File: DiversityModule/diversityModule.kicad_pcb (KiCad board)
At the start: 2 copper layers, 56.5 x 25 mm, 42 parts, among them IC1 LP38798, IC2 TDA1308A, P1 CONN_02X05, P2 CONN_01X03, Q1 BFP840, U1 sn74lvc1g3157, U2 RX5808

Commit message: BOM für beide platinen des kompletten moduls dazugefügt
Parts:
- SMA_E1: footprint PhilippsFootprints:SMA_EDGE_small -> PhilippsFootprints:SMA_EDGE_Johnson_142-0701-801
- moved SMA_E1 0.80 mm to (85.9, 86.7)
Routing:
- net Net-(C15-Pad1): track 5.55 -> 11.3 mm
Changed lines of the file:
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@@
     (links 104)
     (no_connects 0)
-    (area 91.924999 79.924999 148.575001 105.075001)
+    (area 79.159499 79.5 157.35 109.200001)
     (thickness 1.6)
     (drawings 9)
-    (tracks 414)
+    (tracks 418)
     (zones 0)
     (modules 42)
@@
     (34 B.Paste user)
     (35 F.Paste user)
-    (36 B.SilkS user hide)
+    (36 B.SilkS user)
     (37 F.SilkS user)
     (38 B.Mask user)
@@
     (visible_elements FFFEFF7F)
     (pcbplotparams
-      (layerselection 0x00030_ffffffff)
-      (usegerberextensions false)
+      (layerselection 0x014f0_ffffffff)
+      (usegerberextensions true)
       (excludeedgelayer true)
       (linewidth 0.100000)
@@
       (psa4output false)
       (plotreference true)
-      (plotvalue true)
+      (plotvalue false)
       (plotinvisibletext false)
       (padsonsilk false)
-      (subtractmaskfromsilk false)
+      (subtractmaskfromsilk true)
       (outputformat 1)
       (mirror false)
-      (drillshape 1)
+      (drillshape 0)
       (scaleselection 1)
-      (outputdirectory ""))
+      (outputdirectory gerber/))
   )
   (net 0 "")
@@
     )
   )
-  (module PhilippsFootprints:SMA_EDGE_small (layer B.Cu)
-    (at 85.9 85.9 180)
-    (fp_text reference SMA_E1 (at 0 0 180) (layer B.SilkS) hide
-      (effects (font (thickness 0.3048)) (justify mirror))
-    )
-    (fp_text value SMA_EDGE (at 0 -2.54 180) (layer B.SilkS) hide
-      (effects (font (thickness 0.3048)) (justify mirror))
-    )
-    (fp_line (start -6.35 2.5654) (end -6.35 -5.0546) (layer B.SilkS) (width 0.381))
-    (fp_line (start -6.35 -5.0546) (end 6.35 -5.0546) (layer B.SilkS) (width 0.381))
-    (fp_line (start 6.35 -5.0546) (end 6.35 2.5654) (layer B.SilkS) (width 0.381))
-    (fp_line (start 6.35 2.5654) (end -6.35 2.5654) (layer B.SilkS) (width 0.381))
-    (pad 0 connect rect (at -8.8773 1.89484 180) (size 4.572 1.524) (layers *.Cu B.Mask)
-      (net 2 GNDA))
-    (pad 1 connect trapezoid (at -6.858 -1.27 180) (size 0.50038 1.39954) (rect_delta 0.59944 0 ) (layers F.Cu F.Mask)
-      (net 17 "Net-(C15-Pad1)"))
-    (pad 2 connect rect (at -8.8773 -4.42976 180) (size 4.572 1.524) (layers *.Cu B.Mask)
-      (net 2 GNDA))
-    (pad 1 connect rect (at -9.144 -1.27 180) (size 4.07162 1.99898) (layers F.Cu F.Mask)
-      (net 17 "Net-(C15-Pad1)"))
-    (model SMA_EDGE.wrl
-      (at (xyz -0.205 -0.05 -0.12))
-      (scale (xyz 1.3 1.3 1.3))
-      (rotate (xyz 270 0 180))
-    )
-  )
   (module PhilippsFootprints:RX5808 (layer B.Cu)
     (at 124.5 92.7)
@@
     (pad 1 smd rect (at 1.15 2) (size 1.3 2) (layers F.Cu F.Paste F.Mask)
       (net 32 "Net-(RV1-Pad1)"))
+  )
+  (module PhilippsFootprints:SMA_EDGE_Johnson_142-0701-801 (layer B.Cu)
+    (at 85.9 86.7 180)
+    (fp_text reference SMA_E1 (at 0 1.3 180) (layer B.SilkS)
+      (effects (font (thickness 0.3048)) (justify mirror))
+    )
+    (fp_text value SMA_EDGE (at 0 -1.24 180) (layer B.SilkS) hide
+      (effects (font (thickness 0.3048)) (justify mirror))
+    )
+    (fp_line (start -6.2 5.6) (end -6.3 5.6) (layer B.SilkS) (width 0.15))
+    (fp_line (start -6.3 5.6) (end -11.2 5.6) (layer B.SilkS) (width 0.15))
+    (fp_line (start -11.2 5.6) (end -11.2 -5.6) (layer B.SilkS) (width 0.15))
+    (fp_line (start -11.2 -5.6) (end -6.2 -5.6) (layer B.SilkS) (width 0.15))
+    (fp_line (start -6.2 -5.6) (end -6.2 5.6) (layer B.SilkS) (width 0.15))
+    (fp_line (start -6.35 3.8654) (end -6.35 -3.7546) (layer B.SilkS) (width 0.381))
+    (fp_line (start -6.35 -3.7546) (end 6.35 -3.7546) (layer B.SilkS) (width 0.381))
+    (fp_line (start 6.35 -3.7546) (end 6.35 3.8654) (layer B.SilkS) (width 0.381))
+    (fp_line (start 6.35 3.8654) (end -6.35 3.8654) (layer B.SilkS) (width 0.381))
+    (pad 0 connect rect (at -8.9 4.4 180) (size 4.572 2.413) (layers *.Mask F.Cu)
+      (net 2 GNDA))
+    (pad 1 connect trapezoid (at -6.858 0.03 180) (size 0.50038 1.39954) (rect_delta 0.59944 0 ) (layers F.Cu F.Mask)
+      (net 17 "Net-(C15-Pad1)"))
+    (pad 2 connect rect (at -8.9 -4.4 180) (size 4.572 2.413) (layers *.Mask F.Cu)
+      (net 2 GNDA))
+    (pad 1 connect rect (at -9.144 0.03 180) (size 4.07162 2.2) (layers F.Cu F.Mask)
+      (net 17 "Net-(C15-Pad1)"))
+    (model SMA_EDGE.wrl
+      (at (xyz -0.205 -0.05 -0.12))
+      (scale (xyz 1.3 1.3 1.3))
+      (rotate (xyz 270 0 180))
+    )
   )
   (dimension 25 (width 0.3) (layer Cmts.User)
@@
   (segment (start 101.5 90.05) (end 101.5 91) (width 0.15) (layer F.Cu) (net 16))
   (segment (start 105.9 90.55) (end 105.9 90.6) (width 0.15) (layer F.Cu) (net 16))
+  (segment (start 95.044 86.67) (end 96.57 86.67) (width 0.25) (layer F.Cu) (net 17))
+  (segment (start 96.57 86.67) (end 97.1 87.2) (width 0.25) (layer F.Cu) (net 17))
+  (segment (start 97.1 87.2) (end 98.25 87.2) (width 0.25) (layer F.Cu) (net 17))
+  (segment (start 92.758 86.67) (end 95.044 86.67) (width 0.25) (layer F.Cu) (net 17))
   (segment (start 98.25 87.2) (end 95.074 87.2) (width 0.786937) (layer F.Cu) (net 17))
   (segment (start 95.074 87.2) (end 95.044 87.17) (width 0.786937) (layer F.Cu) (net 17))

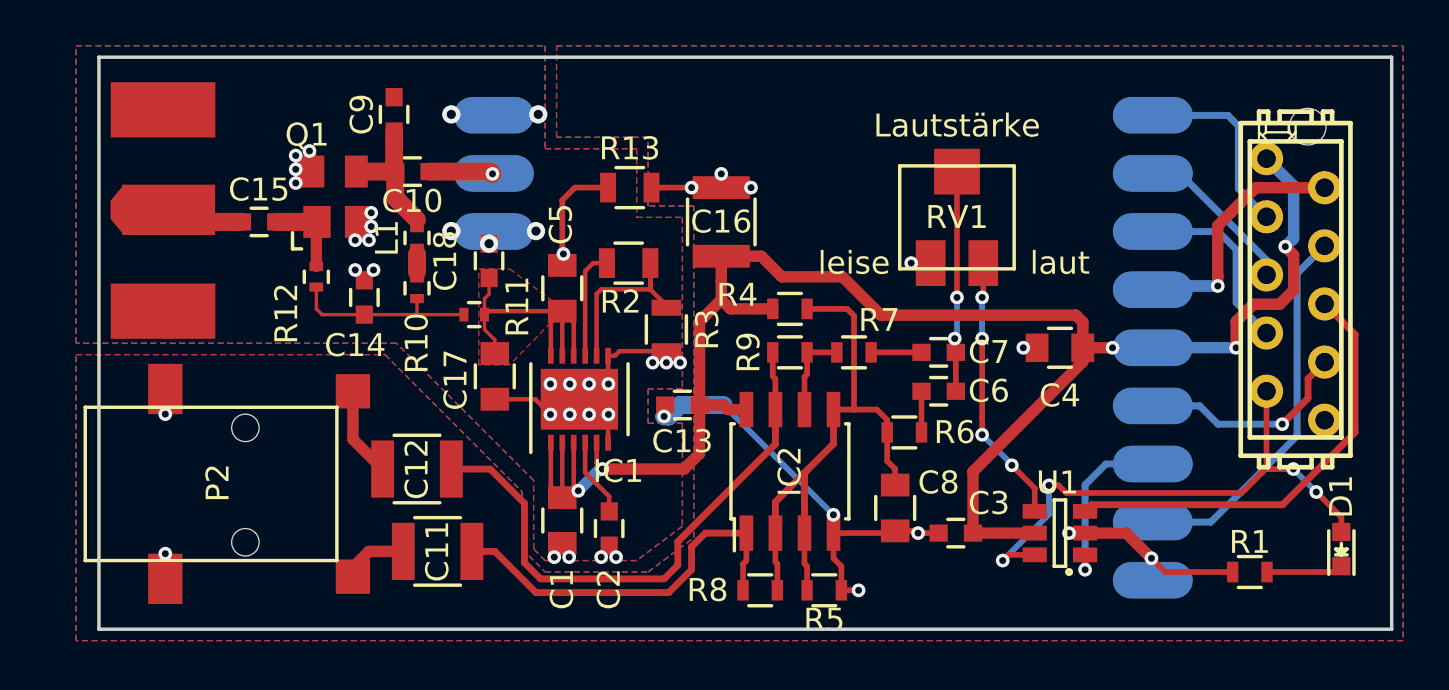
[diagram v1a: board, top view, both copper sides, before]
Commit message: Layoutänderungen für videoumschalter (anderes gehäuse)
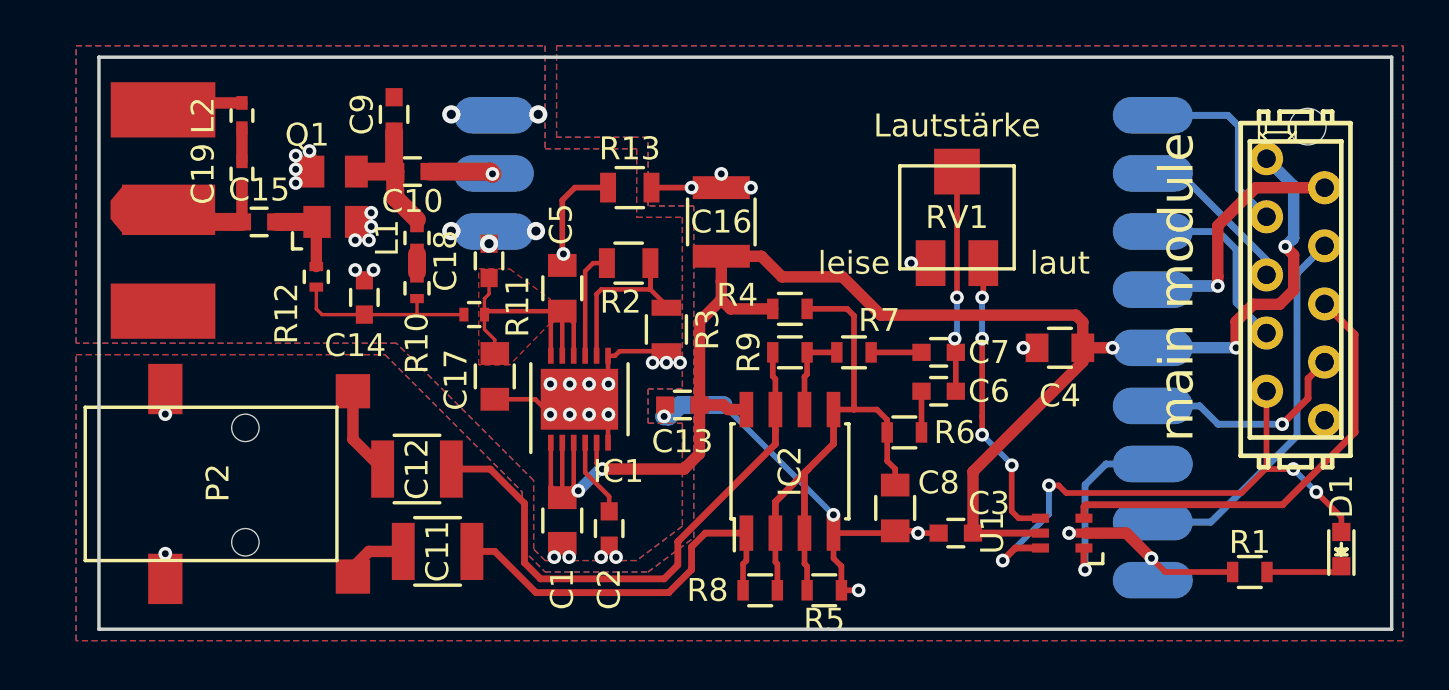
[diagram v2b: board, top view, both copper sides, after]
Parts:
- added C19: 2,2pF, Capacitors_SMD:C_0402, F.Cu at (98.2, 85.1)
- added L2: 1,8nH, Capacitors_SMD:C_0402, F.Cu at (98.2, 82.5)
- U1: footprint TO_SOT_Packages_SMD:SOT-23-6 -> TO_SOT_Packages_SMD:SC-70-6
- moved U1 0.10 mm to (134.1, 100.8), turned to 90 degrees
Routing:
- net GNDA: track 43.1 -> 46.7 mm
- net Net-(C15-Pad1): track 11.3 -> 12.8 mm
- net Net-(C19-Pad2): track 0.00 -> 1.45 mm
- net Net-(RV1-Pad1): track 11.8 -> 12.8 mm
- net /switch: track 23.9 -> 24.6 mm
- net GND: track 47.3 -> 48.0 mm
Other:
- board text added: "main module"

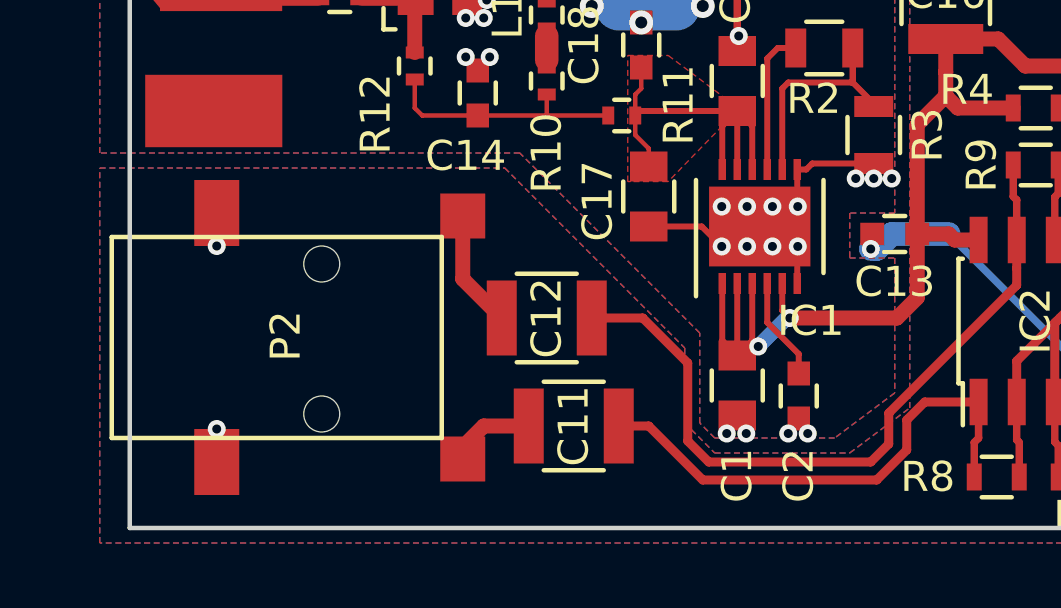
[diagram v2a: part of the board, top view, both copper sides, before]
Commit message: Klinkenbuchse ausgetauscht und zur Lib hinzugefügt.
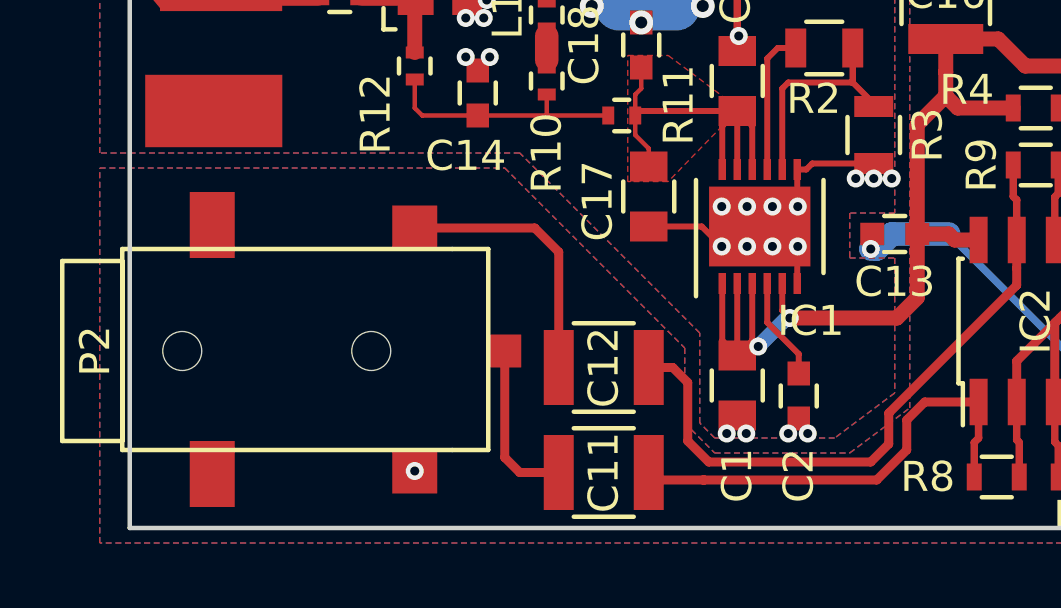
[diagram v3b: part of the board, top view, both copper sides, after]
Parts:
- P2: footprint PhilippsFootprints:LUM1503-SMD -> PhilippsFootprints:LUM1503-03
- moved C12 2.52 mm to (107.8, 99.7)
- moved C11 1.84 mm to (107.8, 103.2)
- moved P2 0.53 mm to (97.3, 99.1)
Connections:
- P2 pad 1: Net-(C12-Pad2) -> GND
- P2 pad 2: GND -> Net-(C11-Pad2)
- P2 pad 3: Net-(C11-Pad2) -> Net-(C12-Pad2)
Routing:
- net Net-(C12-Pad2): track 3.94 -> 8.98 mm
- net Net-(C12-Pad1): track 24.8 -> 21.8 mm
- net Net-(C11-Pad2): track 2.89 -> 5.56 mm
- net GND: track 48.0 -> 45.8 mm, vias 14 -> 13
- net Net-(C11-Pad1): track 17.0 -> 15.4 mm
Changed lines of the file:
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@@
 (kicad_pcb (version 4) (host pcbnew "(2016-06-07 BZR 6887)-product")
   (general
-    (links 107)
+    (links 106)
     (no_connects 0)
-    (area 91.924999 79.924999 148.575001 105.075001)
+    (area 79.159499 79.5 157.500001 109.245001)
     (thickness 1.6)
     (drawings 10)
-    (tracks 428)
+    (tracks 427)
     (zones 0)
     (modules 44)
@@
   )
   (setup
-    (last_trace_width 0.5)
+    (last_trace_width 0.3)
     (user_trace_width 0.15)
     (user_trace_width 0.2)
@@
   )
   (module Capacitors_SMD:C_1210 (layer F.Cu)
-    (at 106.8 101.6 180)
+    (at 107.8 103.15 180)
     (descr "Capacitor SMD 1210, reflow soldering, AVX (see smccp.pdf)")
     (tags "capacitor 1210")
@@
   )
   (module Capacitors_SMD:C_1210 (layer F.Cu)
-    (at 105.9 98 180)
+    (at 107.8 99.65 180)
     (descr "Capacitor SMD 1210, reflow soldering, AVX (see smccp.pdf)")
     (tags "capacitor 1210")
@@
       (net 4 GND))
   )
-  (module PhilippsFootprints:LUM1503-SMD (layer F.Cu)
-    (at 97 98.7)
-    (fp_text reference P2 (at 0.2 -0.1 90) (layer F.SilkS)
-      (effects (font (size 1 1) (thickness 0.15)))
-    )
-    (fp_text value CONN_01X03 (at -0.1 0.06) (layer F.Fab)
-      (effects (font (size 1 1) (thickness 0.15)))
-    )
-    (fp_line (start -5.6 -3.4) (end -5.6 3.3) (layer F.SilkS) (width 0.15))
-    (fp_line (start -5.6 3.3) (end 5.4 3.3) (layer F.SilkS) (width 0.15))
-    (fp_line (start 5.4 3.3) (end 5.4 -3.4) (layer F.SilkS) (width 0.15))
-    (fp_line (start 5.4 -3.4) (end -5.6 -3.4) (layer F.SilkS) (width 0.15))
-    (pad 3 smd rect (at 6.1 4) (size 1.5 1.5) (layers F.Cu F.Paste F.Mask)
-      (net 13 "Net-(C11-Pad2)"))
-    (pad 1 smd rect (at 6.1 -4.1) (size 1.5 1.5) (layers F.Cu F.Paste F.Mask)
-      (net 15 "Net-(C12-Pad2)"))
-    (pad 2 smd rect (at -2.1 4.1) (size 1.5 2.2) (layers F.Cu F.Paste F.Mask)
-      (net 4 GND))
-    (pad 2 smd rect (at -2.1 -4.2) (size 1.5 2.2) (layers F.Cu F.Paste F.Mask)
-      (net 4 GND))
-    (pad "" np_thru_hole circle (at 1.4 -2.5) (size 1.2 1.2) (drill 1.2) (layers *.Cu *.Mask F.SilkS))
-    (pad "" np_thru_hole circle (at 1.4 2.5) (size 1.2 1.2) (drill 1.2) (layers *.Cu *.Mask F.SilkS))
-  )
   (module Resistors_SMD:R_0805 (layer F.Cu)
     (at 115.2 85.7 180)
@@
       (rotate (xyz 0 0 0))
     )
+  )
+  (module PhilippsFootprints:LUM1503-03 (layer F.Cu)
+    (at 97.35 99.1)
+    (fp_text reference P2 (at -6.5 0 90) (layer F.SilkS)
+      (effects (font (size 1 1) (thickness 0.15)))
+    )
+    (fp_text value CONN_01X03 (at 0 1.8) (layer F.Fab)
+      (effects (font (size 1 1) (thickness 0.15)))
+    )
+    (fp_line (start -5.6 0) (end -5.6 -3) (layer F.SilkS) (width 0.15))
+    (fp_line (start -5.6 -3) (end -7.6 -3) (layer F.SilkS) (width 0.15))
+    (fp_line (start -7.6 -3) (end -7.6 3) (layer F.SilkS) (width 0.15))
+    (fp_line (start -7.6 3) (end -5.6 3) (layer F.SilkS) (width 0.15))
+    (fp_line (start -5.6 3) (end -5.6 0) (layer F.SilkS) (width 0.15))
+    (fp_line (start 6.6 3.3) (end 5.4 3.3) (layer F.SilkS) (width 0.15))
+    (fp_line (start 6.6 -3.4) (end 5.4 -3.4) (layer F.SilkS) (width 0.15))
+    (fp_line (start -5.6 -3.4) (end -5.6 3.3) (layer F.SilkS) (width 0.15))
+    (fp_line (start -5.6 3.3) (end 5.4 3.3) (layer F.SilkS) (width 0.15))
+    (fp_line (start 6.6 3.3) (end 6.6 -3.4) (layer F.SilkS) (width 0.15))
+    (fp_line (start 5.4 -3.4) (end -5.6 -3.4) (layer F.SilkS) (width 0.15))
+    (pad 1 smd rect (at 4.15 4) (size 1.5 1.5) (layers F.Cu F.Paste F.Mask)
+      (net 4 GND))
+    (pad 3 smd rect (at 4.15 -4.1) (size 1.5 1.5) (layers F.Cu F.Paste F.Mask)
+      (net 15 "Net-(C12-Pad2)"))
+    (pad NC connect rect (at -2.6 4.1) (size 1.5 2.2) (layers F.Cu F.Mask))
+    (pad NC connect rect (at -2.6 -4.2) (size 1.5 2.2) (layers F.Cu F.Mask))
+    (pad "" np_thru_hole circle (at 2.7 0) (size 1.3 1.3) (drill 1.3) (layers *.Cu *.Mask F.SilkS))
+    (pad "" np_thru_hole circle (at -3.6 0) (size 1.3 1.3) (drill 1.3) (layers *.Cu *.Mask F.SilkS))
+    (pad 2 smd rect (at 7.15 0) (size 1.1 1.1) (layers F.Cu F.Paste F.Mask)
+      (net 13 "Net-(C11-Pad2)"))
   )
   (gr_text "main module" (at 139.1 90.05 90) (layer F.SilkS)
@@
   (segment (start 114.3 99.2) (end 114.3 99.85) (width 0.2) (layer F.Cu) (net 3))
   (segment (start 113.25 98.15) (end 114.3 99.2) (width 0.2) (layer F.Cu) (net 3))
+  (via (at 101.5 103.1) (size 0.6) (drill 0.3) (layers F.Cu B.Cu) (net 4) (status C00000))
   (segment (start 134.4 100.8) (end 135.04992 100.8) (width 0.3) (layer F.Cu) (net 4))
   (segment (start 141.55 102.5) (end 138.6 102.5) (width 0.25) (layer F.Cu) (net 4))
@@
   (segment (start 124.45 102.25) (end 124.45 103.3) (width 0.25) (layer F.Cu) (net 4))
   (segment (start 124.105 101.905) (end 124.45 102.25) (width 0.25) (layer F.Cu) (net 4))
-  (segment (start 94.9 94.5) (end 94.9 95.6) (width 0.5) (layer F.Cu) (net 4))
-  (via (at 94.9 95.6) (size 0.6) (drill 0.3) (layers F.Cu B.Cu) (net 4))
-  (segment (start 94.9 102.8) (end 94.9 101.7) (width 0.5) (layer F.Cu) (net 4))
-  (via (at 94.9 101.7) (size 0.6) (drill 0.3) (layers F.Cu B.Cu) (net 4))
   (segment (start 112.25 91.1) (end 109 91.1) (width 0.2) (layer F.Cu) (net 5))
   (segment (start 109 91.1) (end 108.85 91.25) (width 0.2) (layer F.Cu) (net 5))
@@
   (segment (start 109.22 85.08) (end 109.26 85.08) (width 0.786937) (layer B.Cu) (net 11))
   (segment (start 109.28 85.08) (end 109.26 85.08) (width 0.5) (layer B.Cu) (net 11))
+  (segment (start 111.15 103.4) (end 109.55 103.4) (width 0.3) (layer F.Cu) (net 12) (status 800000))
+  (segment (start 109.55 103.4) (end 109.3 103.15) (width 0.3) (layer F.Cu) (net 12) (status C00000))
   (segment (start 120.295 100.8) (end 120.295 102.005) (width 0.25) (layer F.Cu) (net 12))
   (segment (start 120.15 102.15) (end 120.15 103.3) (width 0.25) (layer F.Cu) (net 12))
   (segment (start 120.295 102.005) (end 120.15 102.15) (width 0.25) (layer F.Cu) (net 12))
   (segment (start 120.295 100.8) (end 118.5 100.8) (width 0.3) (layer F.Cu) (net 12))
-  (segment (start 109.3 101.6) (end 108.3 101.6) (width 0.3) (layer F.Cu) (net 12))
-  (segment (start 111.1 103.4) (end 109.3 101.6) (width 0.3) (layer F.Cu) (net 12))
-  (segment (start 116.9 103.4) (end 111.1 103.4) (width 0.3) (layer F.Cu) (net 12))
+  (segment (start 116.9 103.4) (end 111.15 103.4) (width 0.3) (layer F.Cu) (net 12))
+  (segment (start 111.15 103.4) (end 111.1 103.4) (width 0.3) (layer F.Cu) (net 12))
   (segment (start 117.9 102.4) (end 116.9 103.4) (width 0.3) (layer F.Cu) (net 12))
   (segment (start 117.9 101.4) (end 117.9 102.4) (width 0.3) (layer F.Cu) (net 12))
   (segment (start 118.5 100.8) (end 117.9 101.4) (width 0.3) (layer F.Cu) (net 12))
-  (segment (start 103.1 102.7) (end 103.1 102.3) (width 0.5) (layer F.Cu) (net 13))
-  (segment (start 103.1 102.3) (end 103.8 101.6) (width 0.5) (layer F.Cu) (net 13))
-  (segment (start 103.8 101.6) (end 105.3 101.6) (width 0.5) (layer F.Cu) (net 13))
-  (segment (start 107.4 98) (end 109.1 98) (width 0.3) (layer F.Cu) (net 14))
-  (segment (start 109.1 98) (end 110.6 99.5) (width 0.3) (layer F.Cu) (net 14))
-  (segment (start 110.6 99.5) (end 110.6 102.1) (width 0.3) (layer F.Cu) (net 14))
+  (segment (start 106.3 103.15) (end 105 103.15) (width 0.3) (layer F.Cu) (net 13) (status 400000))
+  (segment (start 104.5 102.65) (end 104.5 99.1) (width 0.3) (layer F.Cu) (net 13) (status 800000))
+  (segment (start 105 103.15) (end 104.5 102.65) (width 0.3) (layer F.Cu) (net 13))
+  (segment (start 109.3 99.65) (end 110.1 99.65) (width 0.3) (layer F.Cu) (net 14) (status 400000))
+  (segment (start 110.1 99.65) (end 110.6 100.15) (width 0.3) (layer F.Cu) (net 14))
+  (segment (start 110.6 100.15) (end 110.6 102.1) (width 0.3) (layer F.Cu) (net 14))
   (segment (start 117.3 102.2) (end 117.3 101.173621) (width 0.3) (layer F.Cu) (net 14))
   (segment (start 110.6 102.1) (end 111.3 102.8) (width 0.3) (layer F.Cu) (net 14))
@@
   (segment (start 121.45 93.95) (end 121.45 92.9) (width 0.25) (layer F.Cu) (net 14))
   (segment (start 121.565 94.065) (end 121.45 93.95) (width 0.25) (layer F.Cu) (net 14))
-  (segment (start 103.1 94.6) (end 103.1 96.7) (width 0.5) (layer F.Cu) (net 15))
-  (segment (start 103.1 96.7) (end 104.4 98) (width 0.5) (layer F.Cu) (net 15))
+  (segment (start 106.3 99.65) (end 106.3 95.8) (width 0.3) (layer F.Cu) (net 15) (status 400000))
+  (segment (start 105.5 95) (end 101.5 95) (width 0.3) (layer F.Cu) (net 15) (status 800000))
+  (segment (start 106.3 95.8) (end 105.5 95) (width 0.3) (layer F.Cu) (net 15))
   (segment (start 103.6 91.25) (end 105.9 91.25) (width 0.15) (layer F.Cu) (net 16))
   (segment (start 105.9 91.25) (end 107.95 91.25) (width 0.15) (layer F.Cu) (net 16))
